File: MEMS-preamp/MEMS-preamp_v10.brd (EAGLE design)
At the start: 51 x 30 mm, 49 parts, among them IC1 BQ297X, IC2 OPA2134UA, IC3 MCP73831, IC4 SC4503, IC5 TPS7A49, IC6 QS6K1, J5 Battery, SW3 SPDT

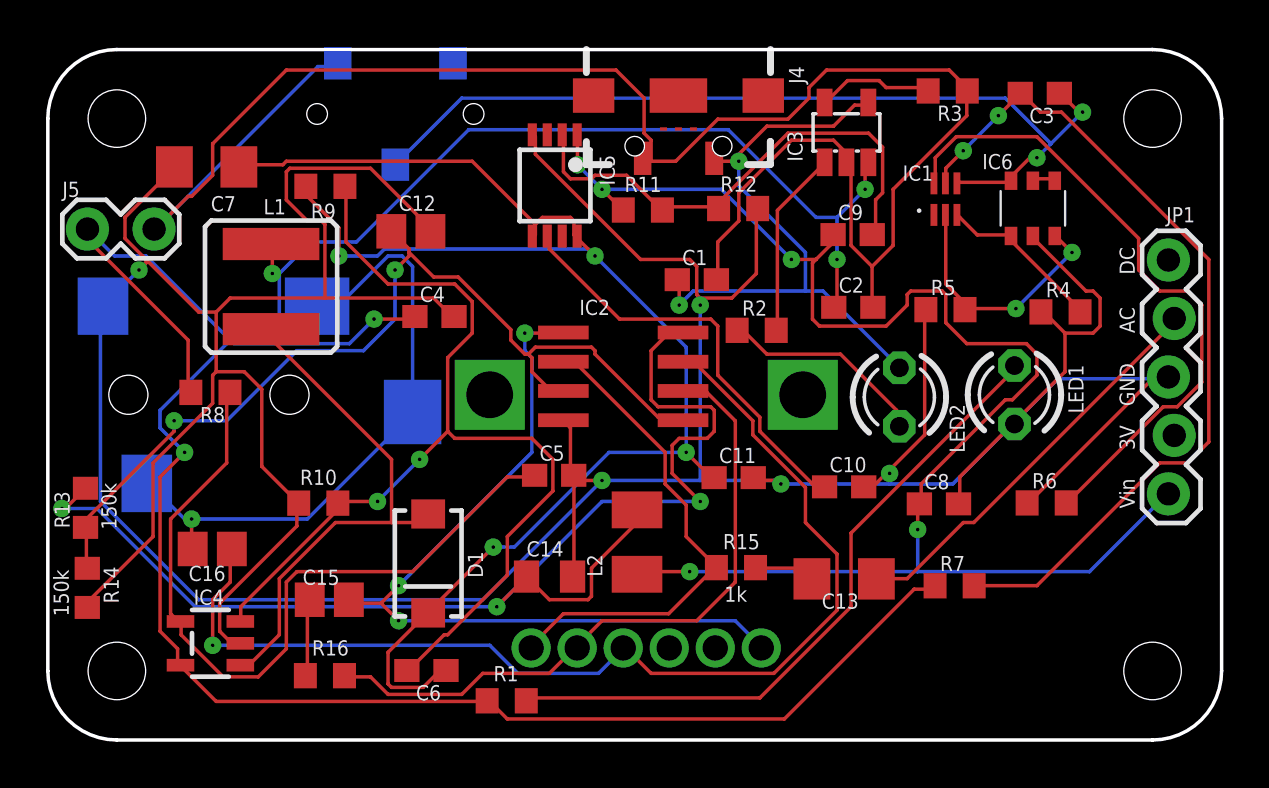
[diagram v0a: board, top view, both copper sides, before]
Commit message: Capacitors changed according to V08
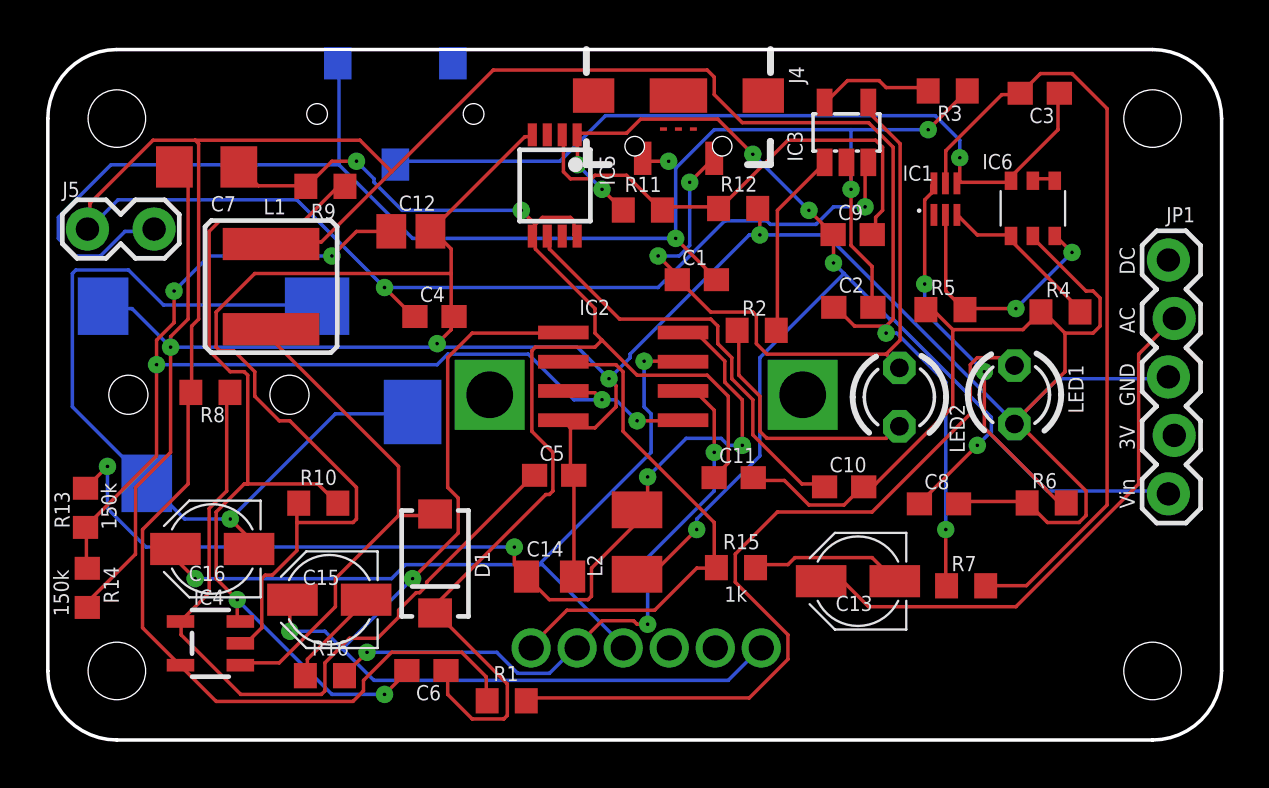
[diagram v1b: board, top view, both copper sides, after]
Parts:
- C13: device rcl:C1206 -> resistor:PANASONIC_B
- C15, C16: device adafruit:C0805 -> resistor:PANASONIC_B
- moved C13 0.61 mm to (35.2, 6.90)
- moved R7 0.50 mm to (39.9, 6.70)
- moved D1 0.30 mm to (16.8, 7.67)
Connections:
- net N$10: now also C16.+; no longer C16.1
- net N$23: now also C13.-; no longer C13.2
- net N$3: now also C13.+; no longer C13.1
- net N$4: now also C15.-; no longer C15.2
- net N$7: now also C16.-; no longer C16.2
- net N$9: now also C15.+; no longer C15.1
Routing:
- net VBAT: track 118.5 -> 153.7 mm, vias 5 -> 4
- net GND: track 199.7 -> 177.8 mm, vias 5 -> 4
- net N$10: track 48.1 -> 34.8 mm, vias 1 -> 2
- net USBGND: track 82.8 -> 70.0 mm, vias 0 -> 4
- net N$34: track 28.3 -> 16.8 mm, vias 0 -> 2
- net N$15: track 55.3 -> 43.8 mm, vias 3 -> 4
- net N$7: track 27.0 -> 37.6 mm
- net N$9: track 35.1 -> 43.7 mm, vias 3 -> 2
- net N$8: track 42.0 -> 50.3 mm, vias 2 -> 5
- net +12V: track 67.8 -> 59.7 mm, vias 5 -> 7
- net N$3: track 17.9 -> 24.3 mm
- net N$2: track 29.3 -> 34.7 mm
- net N$14: track 45.0 -> 39.6 mm
- net V+: track 66.2 -> 61.3 mm, vias 4 -> 2
- net N$23: track 2.65 -> 6.71 mm
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
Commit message: MEMS brd updated for C13, C15 and C16 layer issues
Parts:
- C13, C15, C16: device resistor:PANASONIC_B -> CMU-ArtFab:PANASONIC_B
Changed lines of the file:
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@@
 <attribute name="VALUE" x="14.695" y="20.6" size="0.6604" layer="27" font="vector" ratio="15"/>
 </element>
-<element name="C16" library="resistor" library_urn="urn:adsk.eagle:library:348" package="PANASONIC_B" package3d_urn="urn:adsk.eagle:package:25911/1" value="10uF" x="7.145" y="8.3" smashed="yes" rot="R180">
-<attribute name="NAME" x="7.724" y="7.568" size="0.6604" layer="25" font="vector" ratio="15" rot="R180"/>
-<attribute name="VALUE" x="8.344" y="9.762" size="0.6604" layer="27" font="vector" ratio="15" rot="R180"/>
-</element>
-<element name="C15" library="resistor" library_urn="urn:adsk.eagle:library:348" package="PANASONIC_B" package3d_urn="urn:adsk.eagle:package:25911/1" value="10uF" x="12.23" y="6.095" smashed="yes" rot="R180">
+<element name="C16" library="CMU-ArtFab" package="PANASONIC_B" value="10uF" x="7.145" y="8.3" smashed="yes" rot="R180">
+<attribute name="NAME" x="6.724" y="7.268" size="0.6604" layer="25" font="vector" ratio="15" rot="R180"/>
+<attribute name="VALUE" x="7.644" y="9.762" size="0.6604" layer="27" font="vector" ratio="15" rot="R180"/>
+</element>
+<element name="C15" library="CMU-ArtFab" package="PANASONIC_B" value="10uF" x="12.23" y="6.095" smashed="yes" rot="R180">
 <attribute name="NAME" x="12.679" y="7.399" size="0.6604" layer="25" font="vector" ratio="15" rot="R180"/>
 <attribute name="VALUE" x="13.189" y="5.001" size="0.6604" layer="27" font="vector" ratio="15" rot="R180"/>
@@
 <attribute name="VALUE" x="28.815" y="9.925" size="0.6604" layer="27" font="vector" ratio="15"/>
 </element>
-<element name="C13" library="resistor" library_urn="urn:adsk.eagle:library:348" package="PANASONIC_B" package3d_urn="urn:adsk.eagle:package:25911/1" value="10uF" x="35.2" y="6.9" smashed="yes" rot="R180">
+<element name="C13" library="CMU-ArtFab" package="PANASONIC_B" value="10uF" x="35.2" y="6.9" smashed="yes" rot="R180">
 <attribute name="NAME" x="35.835" y="6.265" size="0.6604" layer="25" font="vector" ratio="15" rot="R180"/>
 <attribute name="VALUE" x="35.835" y="8.805" size="0.6604" layer="27" font="vector" ratio="15" rot="R180"/>
@@
 <element name="SW3" library="CMU-ArtFab" package="SWITCH_SPDT_CL-SB-12B" value="SPDT" x="15.1" y="27.2" smashed="yes" rot="MR180"/>
 <element name="J5" library="SparkFun-Connectors" library_urn="urn:adsk.eagle:library:513" package="1X02_LOCK" value="Battery" x="1.9" y="22.2" smashed="yes">
-<attribute name="NAME" x="0.63" y="23.597" size="0.6604" layer="25" font="vector" ratio="15"/>
-<attribute name="VALUE" x="0.63" y="20.168" size="0.6604" layer="27" font="vector" ratio="15"/>
+<attribute name="G" value="(-)" x="3.7" y="23.6" size="0.6604" layer="27" font="vector" ratio="15"/>
+<attribute name="NAME" x="0.23" y="23.097" size="0.6604" layer="25" font="vector" ratio="15"/>
+<attribute name="P" value="(+)" x="1.2" y="23.6" size="0.6604" layer="27" font="vector" ratio="15"/>
+<attribute name="VALUE" x="0.43" y="20.768" size="0.6604" layer="27" font="vector" ratio="15"/>
 </element>
 <element name="J4" library="CMU-ArtFab" package="USB-B-MICRO-SMD_RED_PASTE" value="" x="27.4" y="28" smashed="yes" rot="R270">
@@
 <wire x1="5.7912" y1="3.2004" x2="5.7649" y2="3.25" width="0.1524" layer="1"/>
 <wire x1="14.6304" y1="19.6596" x2="15.8496" y2="18.4404" width="0.1524" layer="1"/>
-<wire x1="10.8204" y1="23.4696" x2="14.6304" y2="19.6596" width="0.1524" layer="16"/>
-<wire x1="3.048" y1="23.4696" x2="10.8204" y2="23.4696" width="0.1524" layer="16"/>
-<wire x1="1.8288" y1="22.2504" x2="3.048" y2="23.4696" width="0.1524" layer="16"/>
+<wire x1="10.9204" y1="23.4696" x2="14.6304" y2="19.6596" width="0.1524" layer="16"/>
+<wire x1="3.148" y1="23.4696" x2="10.9204" y2="23.4696" width="0.1524" layer="16"/>
+<wire x1="1.8288" y1="22.2504" x2="3.148" y2="23.4696" width="0.1524" layer="16"/>
 <wire x1="15.8496" y1="18.4404" x2="15.95" y2="18.4" width="0.1524" layer="1"/>
 <wire x1="1.8288" y1="22.2504" x2="1.7222" y2="22.2" width="0.1524" layer="16"/>

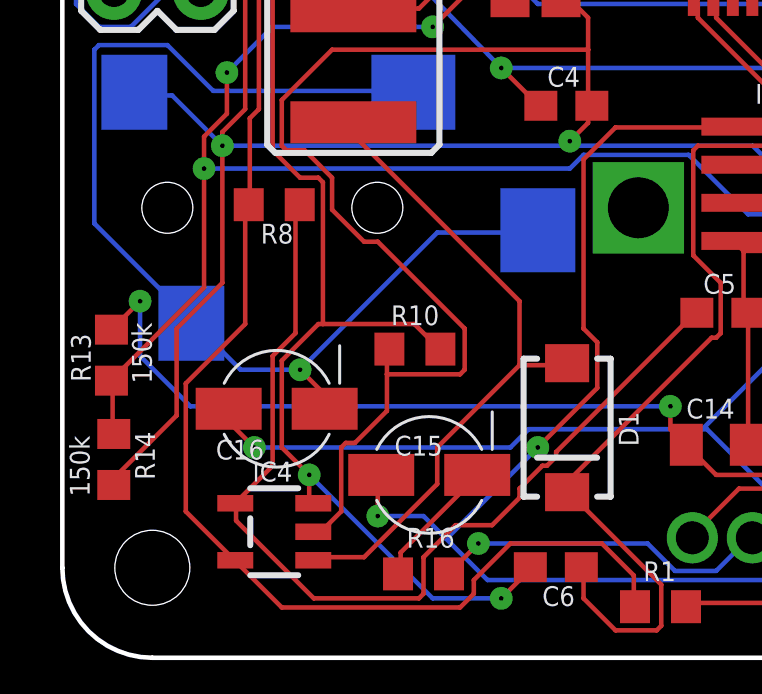
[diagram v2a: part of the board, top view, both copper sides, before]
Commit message: C16 moved away from SC4503
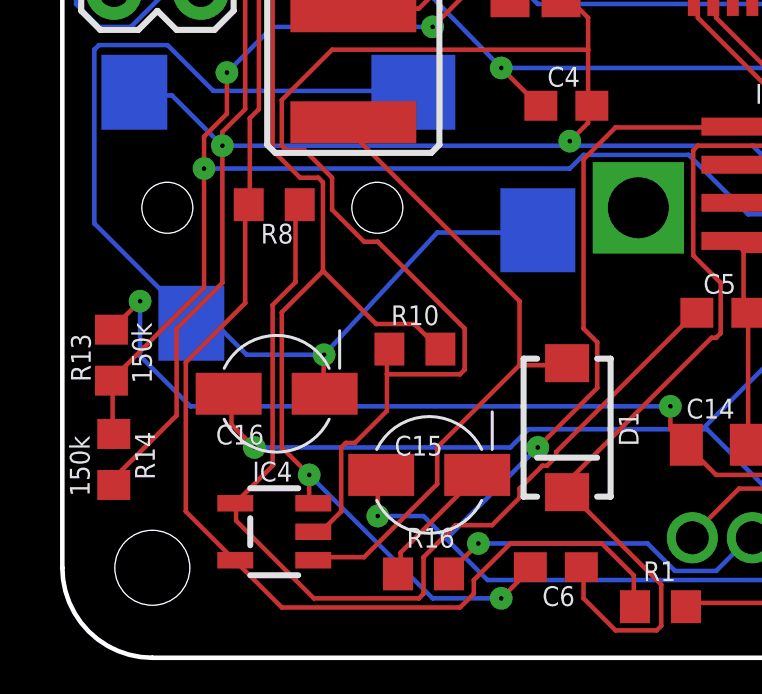
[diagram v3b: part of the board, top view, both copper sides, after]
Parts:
- moved C16 0.50 mm to (7.14, 8.80)
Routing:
- net N$14: track 39.6 -> 40.3 mm
- net N$7: track 37.6 -> 38.2 mm
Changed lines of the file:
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@@
 <attribute name="VALUE" x="14.695" y="20.6" size="0.6604" layer="27" font="vector" ratio="15"/>
 </element>
-<element name="C16" library="CMU-ArtFab" package="PANASONIC_B" value="10uF" x="7.145" y="8.3" smashed="yes" rot="R180">
-<attribute name="NAME" x="6.724" y="7.268" size="0.6604" layer="25" font="vector" ratio="15" rot="R180"/>
-<attribute name="VALUE" x="7.644" y="9.762" size="0.6604" layer="27" font="vector" ratio="15" rot="R180"/>
+<element name="C16" library="CMU-ArtFab" package="PANASONIC_B" value="10uF" x="7.145" y="8.8" smashed="yes" rot="R180">
+<attribute name="NAME" x="6.724" y="7.768" size="0.6604" layer="25" font="vector" ratio="15" rot="R180"/>
+<attribute name="VALUE" x="7.644" y="10.262" size="0.6604" layer="27" font="vector" ratio="15" rot="R180"/>
 </element>
 <element name="C15" library="CMU-ArtFab" package="PANASONIC_B" value="10uF" x="12.23" y="6.095" smashed="yes" rot="R180">
@@
 <contactref element="J3" pad="2"/>
 <wire x1="8.6868" y1="8.8392" x2="8.6868" y2="8.382" width="0.1524" layer="1"/>
-<wire x1="7.9248" y1="9.6012" x2="8.6868" y2="8.8392" width="0.1524" layer="1"/>
-<wire x1="5.9436" y1="9.6012" x2="7.9248" y2="9.6012" width="0.1524" layer="16"/>
-<wire x1="4.4196" y1="11.1252" x2="5.9436" y2="9.6012" width="0.1524" layer="16"/>
-<wire x1="8.6868" y1="8.382" x2="8.745" y2="8.3" width="0.1524" layer="1"/>
-<wire x1="4.4196" y1="11.1252" x2="4.3" y2="11.15" width="0.1524" layer="16"/>
+<wire x1="8.7248" y1="10.1012" x2="8.6868" y2="8.8392" width="0.1524" layer="1"/>
+<wire x1="6.1436" y1="10.1012" x2="8.7248" y2="10.1012" width="0.1524" layer="16"/>
+<wire x1="4.6196" y1="11.6252" x2="6.1436" y2="10.1012" width="0.1524" layer="16"/>
+<wire x1="8.6868" y1="8.382" x2="8.745" y2="8.8" width="0.1524" layer="1"/>
+<wire x1="4.6196" y1="11.6252" x2="4.3" y2="11.15" width="0.1524" layer="16"/>
 <wire x1="5.0292" y1="18.8976" x2="11.5824" y2="18.8976" width="0.1524" layer="16"/>
 <wire x1="3.5052" y1="20.4216" x2="5.0292" y2="18.8976" width="0.1524" layer="16"/>
@@
 <wire x1="4.2672" y1="11.2776" x2="4.3" y2="11.15" width="0.1524" layer="16"/>
 <wire x1="12.4968" y1="14.1732" x2="15.8496" y2="14.1732" width="0.1524" layer="16"/>
-<wire x1="7.9248" y1="9.6012" x2="12.4968" y2="14.1732" width="0.1524" layer="16"/>
+<wire x1="8.7248" y1="10.1012" x2="12.4968" y2="14.1732" width="0.1524" layer="16"/>
 <wire x1="15.8496" y1="14.1732" x2="15.85" y2="14.25" width="0.1524" layer="16"/>
-<via x="7.9248" y="9.6012" extent="1-16" drill="0.1524"/>
+<via x="8.7248" y="10.1012" extent="1-16" drill="0.1524"/>
 </signal>
 <signal name="+12V">
@@
 <wire x1="21.336" y1="7.62" x2="15.5448" y2="7.62" width="0.1524" layer="16"/>
 <wire x1="24.9936" y1="4.1148" x2="21.4884" y2="7.62" width="0.1524" layer="16"/>
-<wire x1="5.6388" y1="8.2296" x2="5.545" y2="8.3" width="0.1524" layer="1"/>
+<wire x1="5.6388" y1="8.2296" x2="5.545" y2="8.8" width="0.1524" layer="1"/>
 <wire x1="24.9936" y1="4.1148" x2="25" y2="4" width="0.1524" layer="16"/>
 <wire x1="25.908" y1="16.4592" x2="27.5844" y2="16.4592" width="0.1524" layer="1"/>
@@
 <wire x1="36.4236" y1="17.9832" x2="36.4236" y2="17.6784" width="0.1524" layer="1"/>
 <wire x1="39.0144" y1="6.7056" x2="39.05" y2="6.7" width="0.1524" layer="1"/>
-<wire x1="6.096" y1="11.1252" x2="6.096" y2="15.0876" width="0.1524" layer="1"/>
-<wire x1="4.1148" y1="9.144" x2="6.096" y2="11.1252" width="0.1524" layer="1"/>
-<wire x1="4.1148" y1="4.8768" x2="4.1148" y2="9.144" width="0.1524" layer="1"/>
+<wire x1="6.096" y1="11.8252" x2="6.096" y2="15.0876" width="0.1524" layer="1"/>
+<wire x1="4.1148" y1="9.844" x2="6.096" y2="11.8252" width="0.1524" layer="1"/>
+<wire x1="4.1148" y1="4.8768" x2="4.1148" y2="9.844" width="0.1524" layer="1"/>
 <wire x1="5.6388" y1="3.3528" x2="4.1148" y2="4.8768" width="0.1524" layer="1"/>
 <wire x1="6.096" y1="15.0876" x2="6.214" y2="15.103" width="0.1524" layer="1"/>
@@
 <contactref element="IC4" pad="4"/>
 <contactref element="C5" pad="1"/>
-<wire x1="7.7724" y1="10.8204" x2="7.7724" y2="15.0876" width="0.1524" layer="1"/>
-<wire x1="7.0104" y1="10.0584" x2="7.7724" y2="10.8204" width="0.1524" layer="1"/>
-<wire x1="7.0104" y1="6.4008" x2="7.0104" y2="10.0584" width="0.1524" layer="1"/>
+<wire x1="7.7724" y1="12.5204" x2="7.7724" y2="15.0876" width="0.1524" layer="1"/>
+<wire x1="7.0104" y1="11.7584" x2="7.7724" y2="12.5204" width="0.1524" layer="1"/>
+<wire x1="7.0104" y1="6.4008" x2="7.0104" y2="11.7584" width="0.1524" layer="1"/>
 <wire x1="5.7912" y1="5.1816" x2="7.0104" y2="6.4008" width="0.1524" layer="1"/>
 <wire x1="7.7724" y1="15.0876" x2="7.914" y2="15.103" width="0.1524" layer="1"/>
@@
 <wire x1="8.2296" y1="5.1816" x2="8.3651" y2="5.15" width="0.1524" layer="1"/>
 <wire x1="11.7348" y1="11.1252" x2="12.4968" y2="10.3632" width="0.1524" layer="1"/>
-<wire x1="8.5344" y1="11.1252" x2="8.6868" y2="11.1252" width="0.1524" layer="1"/>
-<wire x1="8.6868" y1="11.1252" x2="11.7348" y2="11.1252" width="0.1524" layer="1"/>
-<wire x1="7.3152" y1="9.906" x2="8.5344" y2="11.1252" width="0.1524" layer="1"/>
-<wire x1="7.3152" y1="7.0104" x2="7.3152" y2="9.906" width="0.1524" layer="1"/>
 <wire x1="8.2296" y1="6.096" x2="7.3152" y2="7.0104" width="0.1524" layer="1"/>
 <wire x1="12.4968" y1="10.3632" x2="12.602" y2="10.29" width="0.1524" layer="1"/>
@@
 <wire x1="8.5344" y1="16.002" x2="7.9248" y2="16.002" width="0.1524" layer="1"/>
 <wire x1="8.6868" y1="15.8496" x2="8.5344" y2="16.002" width="0.1524" layer="1"/>
-<wire x1="8.6868" y1="11.1252" x2="8.6868" y2="15.8496" width="0.1524" layer="1"/>
 <wire x1="12.8016" y1="23.9268" x2="12.91" y2="24.057" width="0.1524" layer="1"/>
 <via x="14.6304" y="1.9812" extent="1-16" drill="0.1524"/>
 <via x="8.2296" y="6.096" extent="1-16" drill="0.1524"/>
+<wire x1="8.6868" y1="12.8868" x2="8.6868" y2="12.9" width="0.1524" layer="1"/>
+<wire x1="8.6868" y1="12.9" x2="8.6868" y2="15.8496" width="0.1524" layer="1"/>
+<wire x1="7.3152" y1="7.0104" x2="7.3152" y2="11.5152" width="0.1524" layer="1"/>
+<wire x1="7.3152" y1="11.5152" x2="8.6868" y2="12.8868" width="0.1524" layer="1"/>
+<wire x1="8.6868" y1="12.9" x2="10.4616" y2="11.1252" width="0.1524" layer="1"/>
+<wire x1="10.4616" y1="11.1252" x2="11.7348" y2="11.1252" width="0.1524" layer="1"/>
 </signal>
 <signal name="V+">
